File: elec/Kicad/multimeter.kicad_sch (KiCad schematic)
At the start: 0 parts

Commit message: multimetring
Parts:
- added R18, R21: 9996, symbol Device:R
- added R22, R23: 833, symbol Device:R
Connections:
- new net: R18.2, R23.1
- new net: R21.2, R22.2
- new net GND: R22.1, R23.2
- new net read_pin_high: R21.1
- new net read_pin_low: R18.1
- no-connect marks 0 -> 2

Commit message: multimetrie
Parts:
- removed R18, R21: 9996, symbol Device:R
- added D4, D5: PESD5V5C1ULYL, PESD5V5C1ULYL:DIO_PESD5V5C1ULYL, symbol PESD5V5C1ULYL:PESD5V5C1ULYL
- added F1, F2: F0603G0R03FNTR, F0603G0R03FNTR, symbol F0603G0R03FNTR:F0603G0R03FNTR
- added J3: HX0201800000G, HX0201800000G, symbol HX0201800000G:HX0201800000G
- added R24, R25: 9996, symbol Device:R
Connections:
- net GND: now also D4.A, D5.A
- net read_pin_high: now also F1.2
- net read_pin_low: now also F2.2
- net at R23.1: now also D4.K, F2.1, R25.1
- net at R22.2: now also D5.K, F1.1, R24.1
- new net: J3.2, R24.2
- new net: J3.4, R25.2
- no-connect marks 2 -> 0
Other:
- moved on the sheet: R22, R23

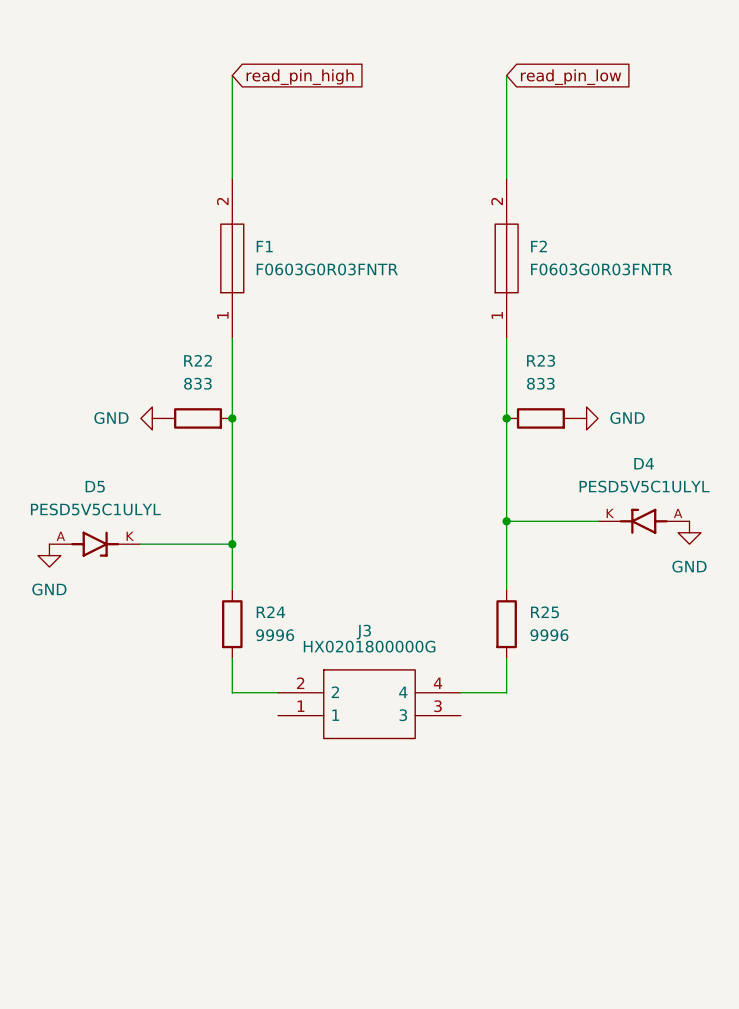
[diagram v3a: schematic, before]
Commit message: manque h-bridge
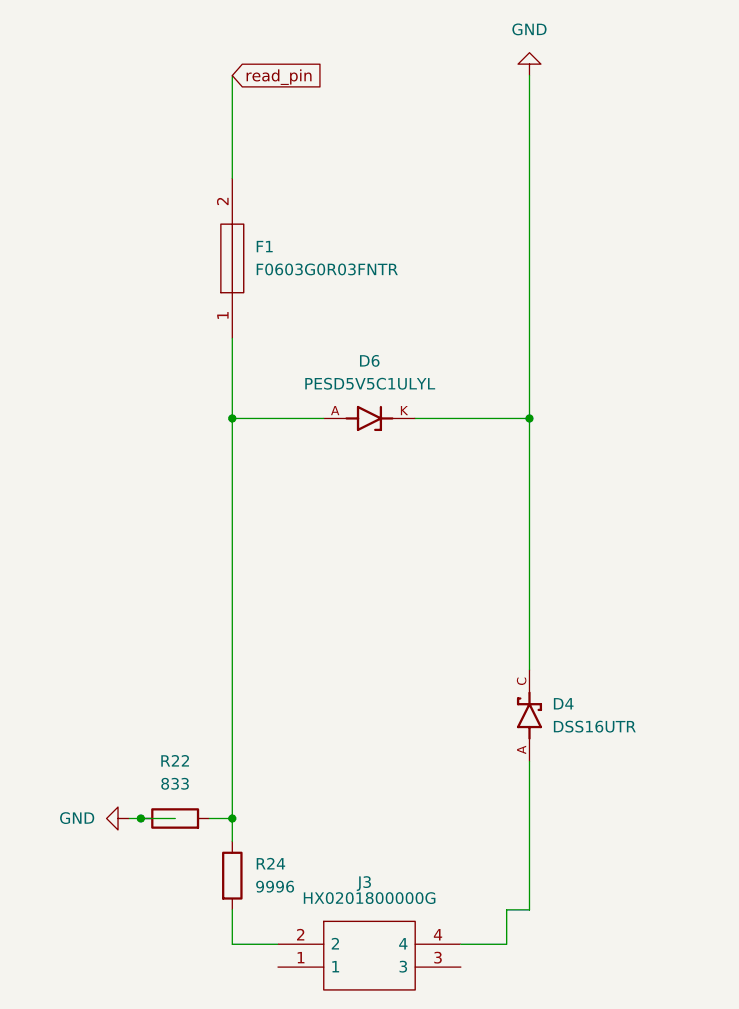
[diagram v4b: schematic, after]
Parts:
- removed D4, D5: PESD5V5C1ULYL, PESD5V5C1ULYL:DIO_PESD5V5C1ULYL, symbol PESD5V5C1ULYL:PESD5V5C1ULYL
- removed F2: F0603G0R03FNTR, F0603G0R03FNTR, symbol F0603G0R03FNTR:F0603G0R03FNTR
- removed R23: 833, symbol Device:R
- removed R25: 9996, symbol Device:R
- added D4: DSS16UTR, DSS16UTR:SODFL3618X110N, symbol DSS16UTR:DSS16UTR
- added D6: PESD5V5C1ULYL, PESD5V5C1ULYL:DIO_PESD5V5C1ULYL, symbol PESD5V5C1ULYL:PESD5V5C1ULYL
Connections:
- net GND: now also D4.C, D6.K
- net at J3.4: now also D4.A
- net at F1.1, R22.2, R24.1: now also D6.A
- net read_pin_high renamed read_pin
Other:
- moved on the sheet: J3, R22, R24

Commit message: add a few footprint
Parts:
- R22, R24: footprint (none) -> Resistor_SMD:R_0603_1608Metric_Pad0.98x0.95mm_HandSolder
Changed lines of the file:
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@@
 			)
 		)
-		(property "Footprint" ""
+		(property "Footprint" "Resistor_SMD:R_0603_1608Metric_Pad0.98x0.95mm_HandSolder"
 			(at 30.48 113.538 90)
 			(effects
@@
 			)
 		)
-		(property "Footprint" ""
+		(property "Footprint" "Resistor_SMD:R_0603_1608Metric_Pad0.98x0.95mm_HandSolder"
 			(at 35.052 118.11 90)
 			(effects

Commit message: modif pour charly
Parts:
- F1: footprint F0603G0R03FNTR -> F0603G0R03FNTR:F0603G0R03FNTR
- J3: footprint HX0201800000G -> HX0201800000G:HX0201800000G
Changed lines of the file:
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@@
 			)
 		)
-		(property "Footprint" "HX0201800000G"
+		(property "Footprint" "HX0201800000G:HX0201800000G"
 			(at 58.42 123.19 0)
 			(effects
@@
 			)
 		)
-		(property "Footprint" "F0603G0R03FNTR"
+		(property "Footprint" "F0603G0R03FNTR:F0603G0R03FNTR"
 			(at 35.56 44.45 0)
 			(effects
